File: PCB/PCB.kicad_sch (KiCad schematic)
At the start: 30 parts, among them J1 Conn_01x06_Pin, U2 A7106, U3 HT7333-3.3V, U4 STM32G031F6Px, Y1 16MHz

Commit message: Update BOM and simplifiy board
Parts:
- removed C13, C14, C5: 100nF, Capacitor_SMD:C_0402_1005Metric, symbol Device:C
- J1: footprint Connector_PinHeader_2.54mm:PinHeader_1x06_P2.54mm_Vertical -> Connector_PinHeader_2.54mm:PinHeader_1x06_P2.54mm_Horizontal
- L2, L3: footprint (none) -> Inductor_SMD:L_0402_1005Metric

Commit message: Update schematic
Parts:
- U3: value HT7333-3.3V -> HT7333-3.3v; LCSC C84207 -> C527569
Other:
- moved on the sheet: U3

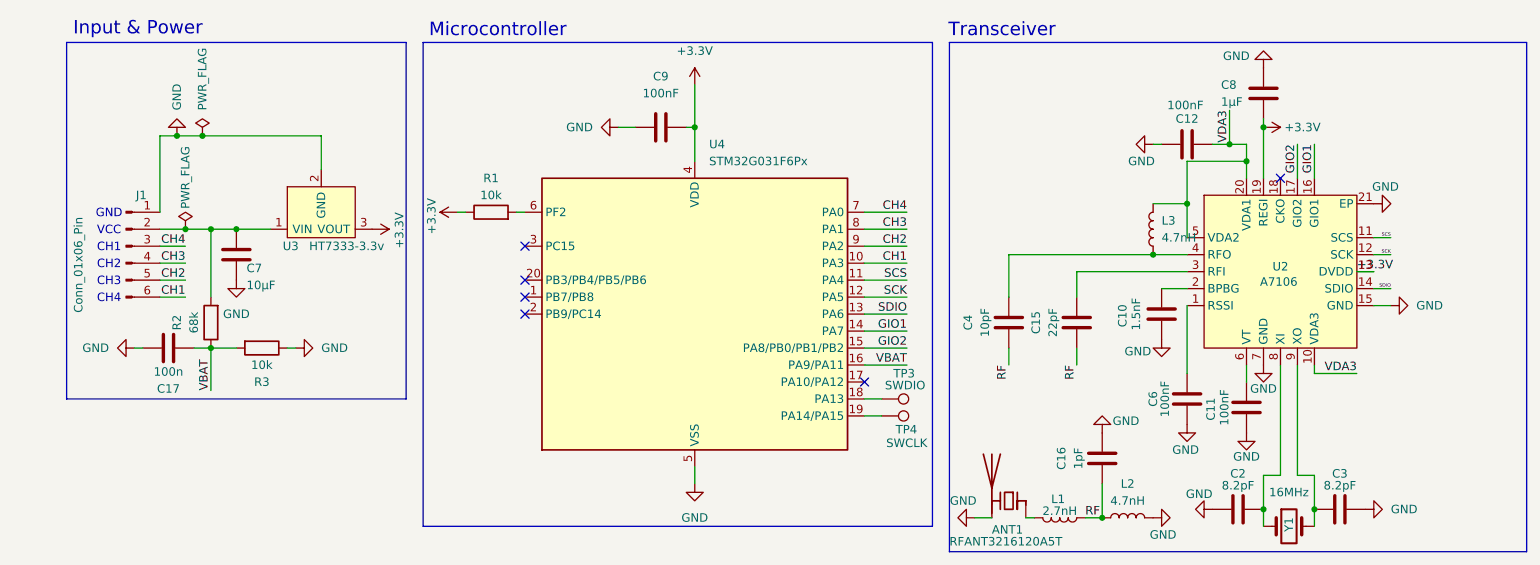
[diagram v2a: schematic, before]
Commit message: Add LED and new LDO
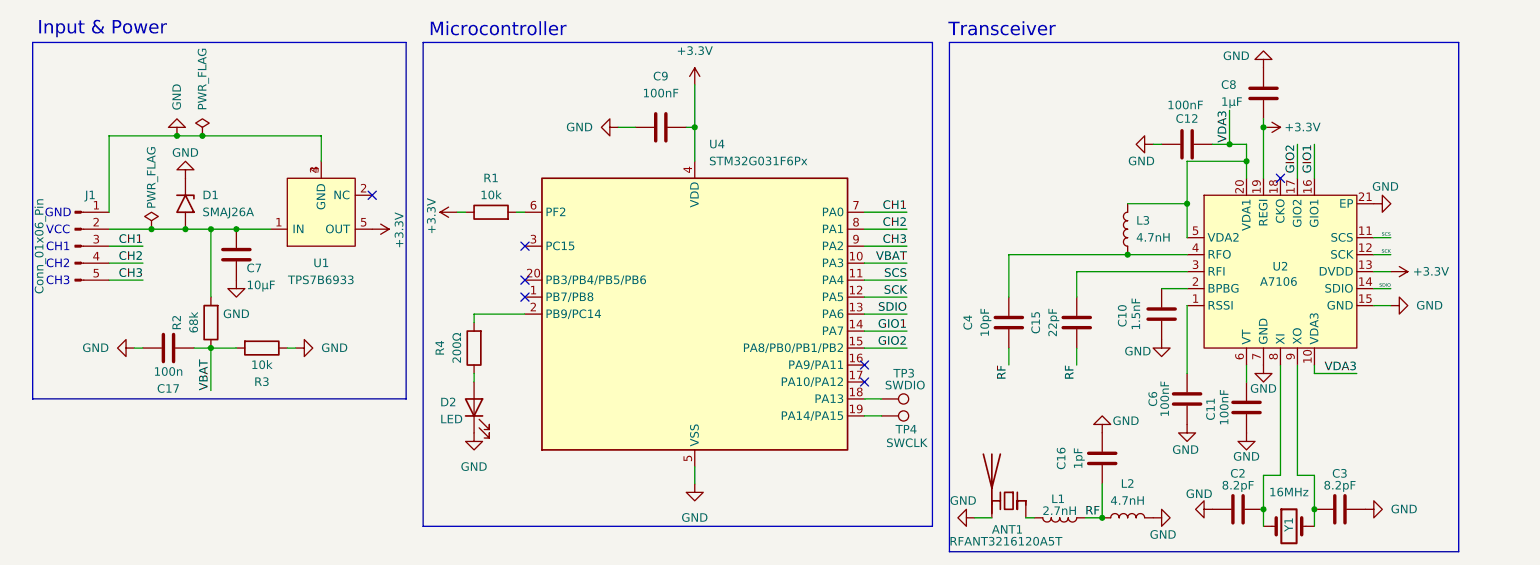
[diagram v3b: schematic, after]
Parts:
- removed U3: HT7333-3.3v, Package_TO_SOT_SMD:SOT-89-3, symbol Nano2A:HT7333
- added D1: SMAJ26A, Diode_SMD:D_SMA, symbol Diode:SMAJ26A
- added D2: LED, LED_SMD:LED_0603_1608Metric, symbol Device:LED
- added R4: 200Ω, Resistor_SMD:R_0402_1005Metric, symbol Device:R
- added U1: TPS7B6933, Package_TO_SOT_SMD:SOT-23-5, symbol Nano2A:TPS7B6933
- J1: footprint Connector_PinHeader_2.54mm:PinHeader_1x06_P2.54mm_Horizontal -> Connector_PinHeader_2.54mm:PinHeader_1x05_P2.54mm_Horizontal; symbol Connector:Conn_01x06_Pin -> Connector:Conn_01x05_Pin
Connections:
- net CH4 is gone; now on net CH1: J1.3 (Pin_3), U4.7 (PA0)
- net +3.3V: now also U1.5 (OUT)
- net CH1: no longer J1.6 (Pin_6), U4.10 (PA3)
- net CH2: now also J1.4 (Pin_4), U4.8 (PA1); no longer J1.5 (Pin_5), U4.9 (PA2)
- net CH3: now also J1.5 (Pin_5), U4.9 (PA2); no longer J1.4 (Pin_4), U4.8 (PA1)
- net GND: now also D1.1 (A1), D2.1 (K), U1.3 (GND), U1.4 (GND)
- net VBAT: now also U4.10 (PA3); no longer U4.16 (PA9/PA11)
- net at U4.2 (PB9/PC14): now also R4.2
- net at C7.2, J1.2 (Pin_2), R2.2: now also D1.2 (A2), U1.1 (IN)
- new net: D2.2 (A), R4.1
- no-connect marks 6 -> 7
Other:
- note removed: "CH4"
- moved on the sheet: L3

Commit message: Update public information and crystal
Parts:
- J1: value Conn_01x06_Pin -> Conn_01x05_Pin
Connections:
- net CH2: now also J1.2 (Pin_2); no longer J1.4 (Pin_4)
- net CH3: now also J1.1 (Pin_1); no longer J1.5 (Pin_5)
- net GND: now also J1.5 (Pin_5); no longer J1.1 (Pin_1)
- net at C7.2, D1.2 (A2), R2.2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: now also J1.4 (Pin_4); no longer J1.2 (Pin_2)
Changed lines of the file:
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@@
 	)
 	(junction
+		(at 64.77 57.15)
+		(diameter 0)
+		(color 0 0 0 0)
+	)
+	(junction
 		(at 46.99 71.12)
 		(diameter 0)
@@
 	(wire
 		(pts
-			(xy 49.53 57.15) (xy 67.31 57.15)
+			(xy 49.53 57.15) (xy 64.77 57.15)
 		)
 		(stroke
@@
 	(wire
 		(pts
+			(xy 64.77 57.15) (xy 67.31 57.15)
+		)
+		(stroke
+			(width 0)
+			(type default)
+		)
+	)
+	(wire
+		(pts
 			(xy 35.56 78.74) (xy 40.64 78.74)
 		)
@@
 	(wire
 		(pts
+			(xy 64.77 57.15) (xy 64.77 60.96)
+		)
+		(stroke
+			(width 0)
+			(type default)
+		)
+	)
+	(wire
+		(pts
 			(xy 203.2 58.42) (xy 200.66 58.42)
 		)
@@
 		)
 		(property "Footprint" "Crystal:Crystal_SMD_3225-4Pin_3.2x2.5mm"
-			(at 212.09 115.57 0)
+			(at 211.836 124.46 0)
 			(hide yes)
 			(show_name no)
@@
 		)
 		(property "Description" "Two pin crystal"
-			(at 212.09 115.57 0)
+			(at 212.09 121.92 0)
 			(hide yes)
 			(show_name no)
@@
 		)
 		(property "LCSC" "C13738"
-			(at 212.09 115.57 0)
+			(at 211.582 119.38 0)
 			(hide yes)
 			(show_name no)
@@
 		(lib_id "Connector:Conn_01x05_Pin")
 		(at 30.48 73.66 0)
+		(mirror x)
 		(unit 1)
 		(body_style 1)
@@
 		(dnp no)
 		(property "Reference" "J1"
-			(at 32.766 66.04 0)
+			(at 27.94 66.294 0)
 			(show_name no)
 			(do_not_autoplace no)
@@
 			)
 		)
-		(property "Value" "Conn_01x06_Pin"
+		(property "Value" "Conn_01x05_Pin"
 			(at 25.146 73.66 90)
 			(show_name no)

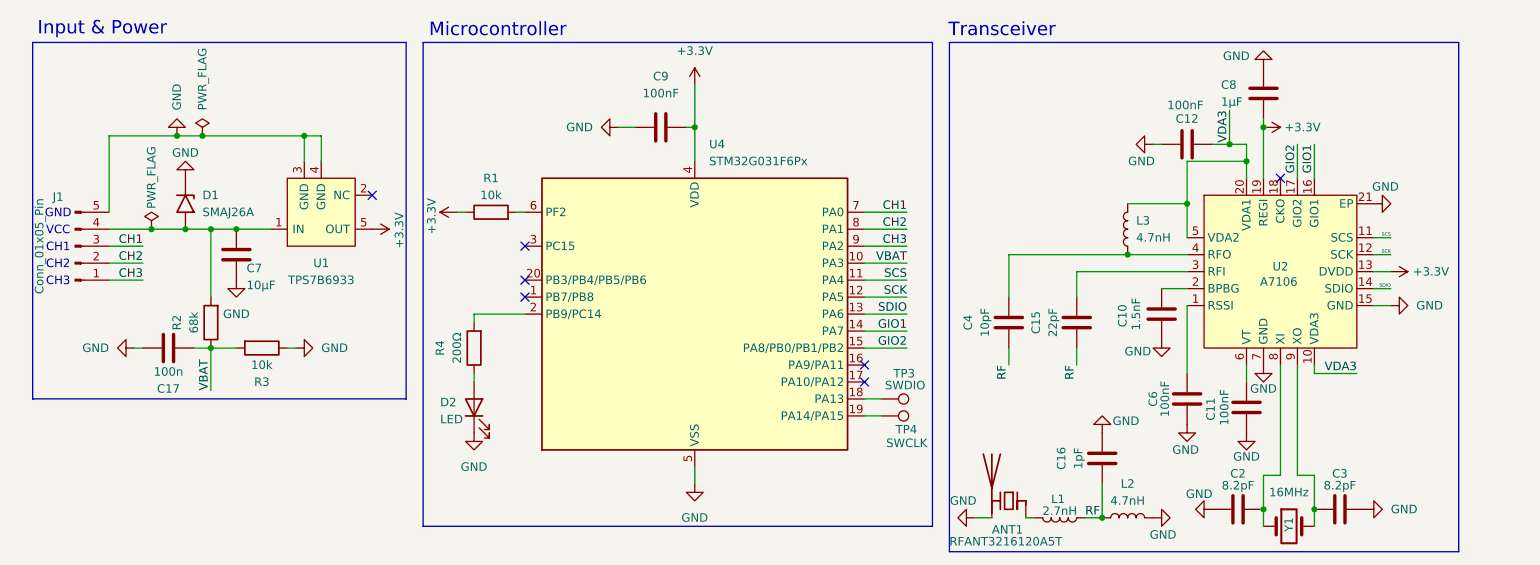
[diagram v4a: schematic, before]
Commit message: Replace MCU
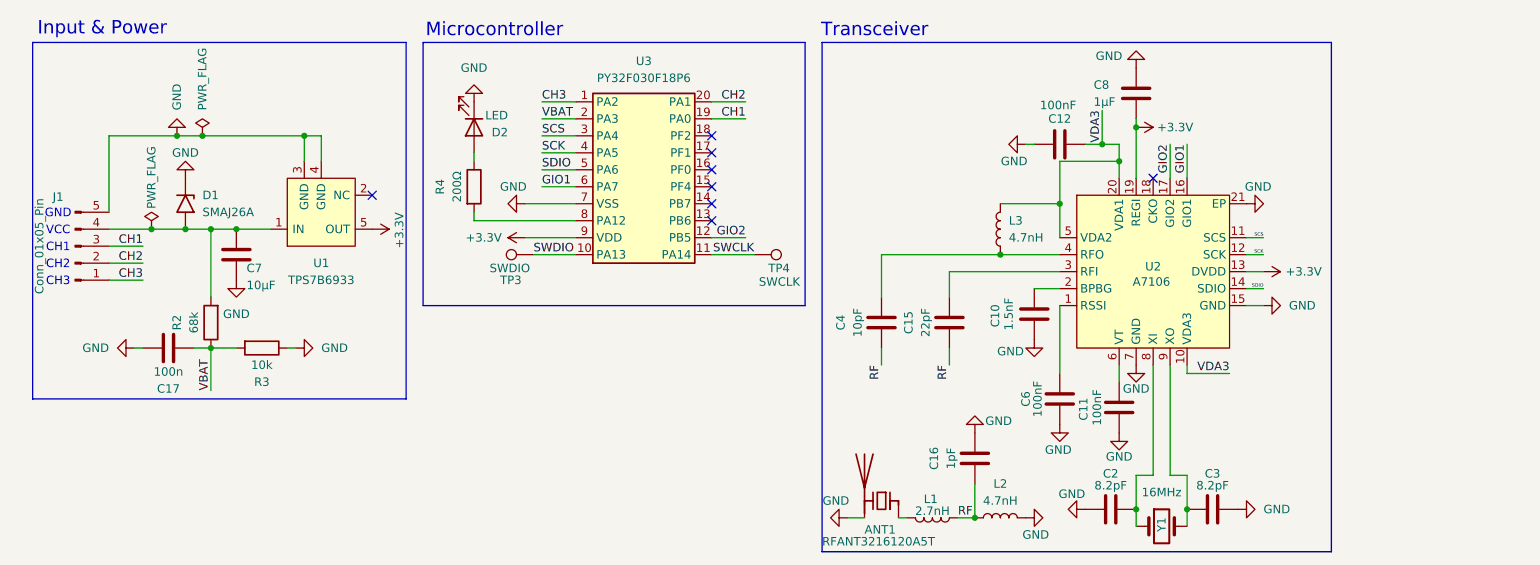
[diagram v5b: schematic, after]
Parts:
- removed C9: 100nF, Capacitor_SMD:C_0402_1005Metric, symbol Device:C
- removed R1: 10k, Resistor_SMD:R_0402_1005Metric, symbol Device:R
- removed U4: STM32G031F6Px, Package_SO:TSSOP-20_4.4x6.5mm_P0.65mm, symbol MCU_ST_STM32G0:STM32G031F6Px
- added U3: PY32F030F18P6, symbol Nano2A:PY32F030F18P6
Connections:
- net +3.3V: now also U3.9 (VDD)
- net CH1: now also U3.19 (PA0)
- net CH2: now also U3.20 (PA1)
- net CH3: now also U3.1 (PA2)
- net GIO1: now also U3.6 (PA7)
- net GIO2: now also U3.12 (PB5)
- net GND: now also U3.7 (VSS)
- net SCK: now also U3.4 (PA5)
- net SCS: now also U3.3 (PA4)
- net SDIO: now also U3.5 (PA6)
- net VBAT: now also U3.2 (PA3)
- net SWDIO: now reaches TP3.1
- net SWDIO: now also U3.10 (PA13)
- net SWCLK: now reaches TP4.1
- net SWCLK: now also U3.11 (PA14)
- net at R4.2: now also U3.8 (PA12)
- no-connect marks 7 -> 8
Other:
- moved on the sheet: ANT1, C10, C11, C12, C15, C16, C2, C3, C4, C6, C8, D2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

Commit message: Schematic fixes
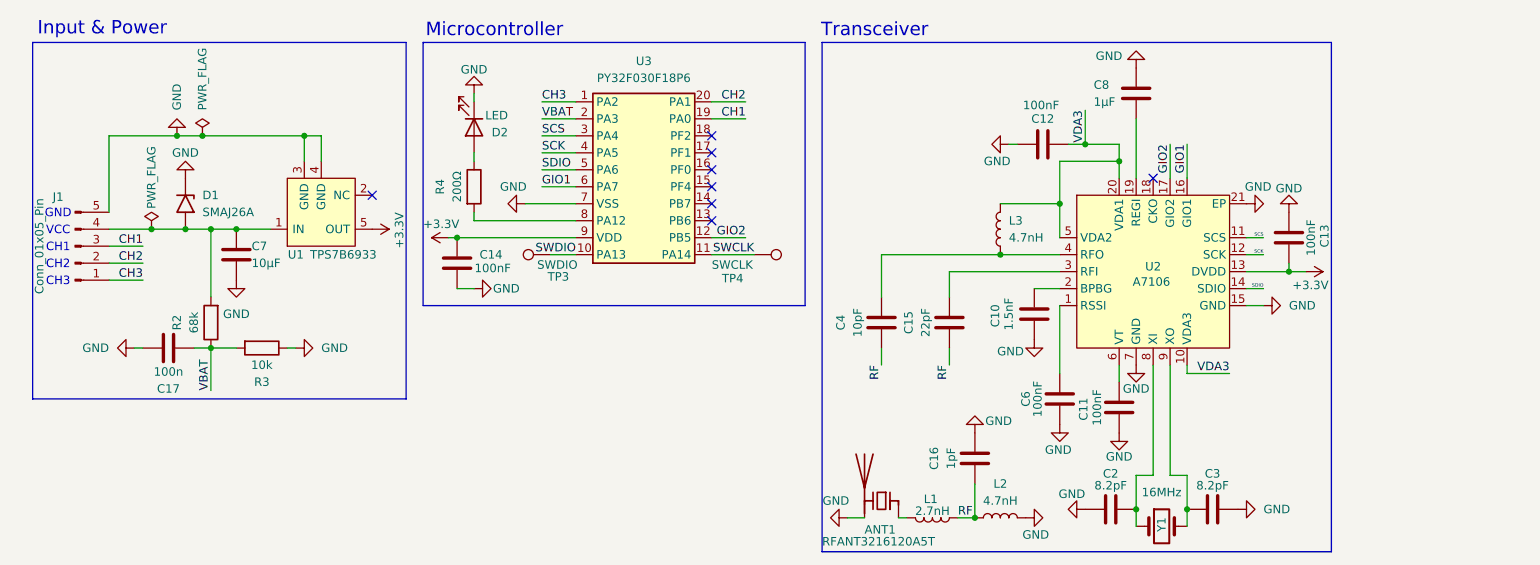
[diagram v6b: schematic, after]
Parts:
- added C13, C14: 100nF, Capacitor_SMD:C_0402_1005Metric, symbol Device:C
- U3: footprint (none) -> Package_SO:TSSOP-20_4.4x6.5mm_P0.65mm
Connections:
- net +3.3V: now also C13.1, C14.1; no longer C8.2, U2.19 (REGI)
- net GND: now also C13.2, C14.2
- new net: C8.2, U2.19 (REGI)
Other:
- moved on the sheet: C12, TP3
